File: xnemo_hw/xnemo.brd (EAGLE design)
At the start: 49.9 x 49 mm, 40 parts, among them J1 MICRO_USB_B_RECEPT, J2 DM3D_MICRO_SD, J3 HEADER_2X5_0.05_SMD, J4 HEADER_2X5_0.05_THRU, J5 HEADER_2X5_0.05_THRU, U1 LTC3559, U2 L3GD20, U3 STM32F405RG, U4 STM32F407VE, U5 HMC5883L, U6 ADXL345, X1 TXC_7A_XTAL

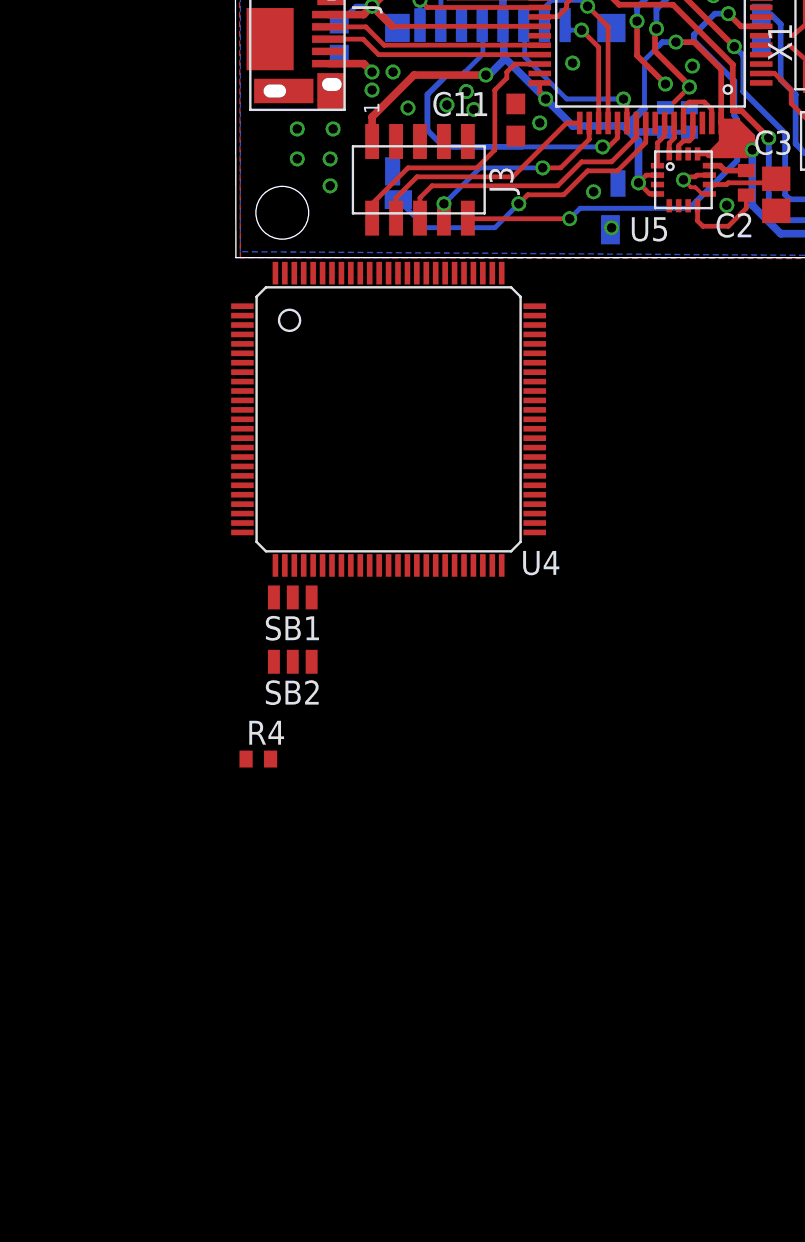
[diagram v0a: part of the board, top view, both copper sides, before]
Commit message: More junk added -- 2 compass units...
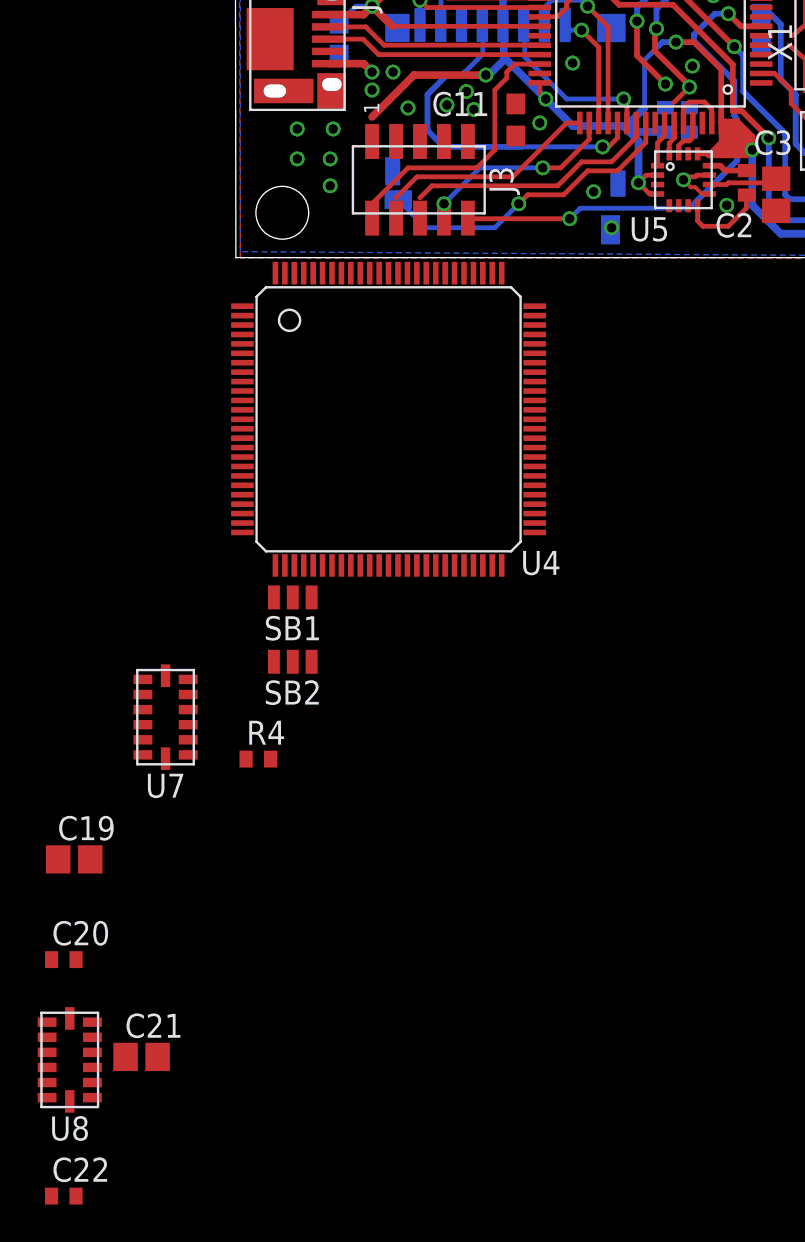
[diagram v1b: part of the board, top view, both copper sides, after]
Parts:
- added C19, C21: 4.7u, resistor:C0805
- added C20, C22: 0.22u, resistor:C0402
- added U7, U8: LSM303DLHC, xnemo:ST_LGA14_3X5
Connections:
- net N$1 renamed PDR_ON
- net N$16 renamed USART3_RX
- net N$17 renamed USART3_TX
- net N$18 renamed SPI2_MOSI
- net N$19 renamed SPI2_MISO
- net N$20 renamed SPI2_SCK
- net N$26 renamed I2S3_WS
- net N$39 renamed SPI1_MISO
- net N$40 renamed SPI1_MOSI
- net N$45 renamed DCMI_D2
- net N$46 renamed DCMI_D3
- net N$49 renamed DCMI_D4
- net N$50 renamed DCMI_D6
- net N$51 renamed DCMI_D7
- net N$68 renamed USART2_TX
- net N$69 renamed USART2_RX
- net N$72 renamed DCMI_HSYNC
- net N$73 renamed SPI1_SCK
- net N$74 renamed DCMI_PIXCLK
- net N$9 renamed DCMI_D0
- removed net N$2: U4.P$96
- removed net N$22: U4.P$72
- removed net N$25: U4.P$76
- removed net N$29: U4.P$80
- removed net N$32: U4.P$83
- removed net N$38: U4.P$89
- removed net N$4: U4.P$68
- removed net N$44: U4.P$95
- removed net N$56: U4.P$10
- removed net N$57: U4.P$11
- removed net N$90: U4.P$47
- removed net N$91: U4.P$48
- removed net SD_DAT0: J2.P$2, U3.P$39
- removed net SD_DAT1: J2.P$1, U3.P$40
- new net COMP1_DRDY: U7.P$9
- new net COMP1_INT1: U7.P$4
- new net COMP1_INT2: U7.P$5
- new net COMP2_DRDY: U8.P$9
- new net COMP2_INT1: U8.P$4
- new net COMP2_INT2: U8.P$5
- new net DCMI_D5: U4.P$92
- new net DCMI_VSYNC: U4.P$93
- new net I2C1_SCL: R6.1, U4.P$95, U7.P$2
- new net I2C1_SDA: R5.1, U4.P$96, U7.P$3
- new net I2C2_SCL: U4.P$47, U8.P$2
- new net I2C2_SDA: U4.P$48, U8.P$3
- new net N$23: C22.1, U8.P$13
- new net N$52: C19.2, U7.P$6
- new net NC: J3.7
- new net NRESET: J3.9, U4.P$14
- new net SD_DAT0_I2C3_SCL: J2.P$2, U3.P$39, U4.P$65
- new net SD_DAT1_I2C3_SDA: J2.P$1, U3.P$40, U4.P$66
- new net SWDCLK: J3.3, U4.P$76
- new net SWDIO: J3.1, U4.P$72
- new net SWO: J3.5, U4.P$89
- net 3V3: now also J3.2, U4.P$11, U7.P$1, U7.P$14, U8.P$1, U8.P$14; no longer J3.1
- net GND: now also C19.1, C21.1, J3.10, J3.4, J3.6, J3.8, U4.P$10, U7.P$10, U7.P$11, U7.P$7, U8.P$10, U8.P$11, U8.P$7; no longer J3.3, J3.5, J3.7, J3.9
- net I2C_SCL: no longer R6.1, U4.P$92
- net I2C_SDA: no longer R5.1, U4.P$93
- net JTCK: no longer J3.4
- net JTDI: no longer J3.8
- net JTDO: no longer J3.6
- net JTMS: no longer J3.2
- net N$27: now also C20.1, U7.P$13; no longer U4.P$78
- net N$28: now also C21.2, U8.P$6; no longer U4.P$79
- net N$6: now also C22.2, U8.P$12; no longer U4.P$66
- net N$7: now also C20.2, U7.P$12; no longer U4.P$65
- net RESET: no longer J3.10, U4.P$14
- net SD_CLK: now also U4.P$80
- net SD_CMD: now also U4.P$83
- net SD_DAT2: now also U4.P$78
- net SD_DAT3: now also U4.P$79
- net VUSB: now also U4.P$68
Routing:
- net SD_DAT1_I2C3_SDA: track 0.00 -> 7.83 mm, vias 0 -> 1
- net SD_DAT1: track 7.83 -> 0.00 mm, vias 1 -> 0
- net SD_DAT0_I2C3_SCL: track 0.00 -> 7.19 mm, vias 0 -> 1
- net SD_DAT0: track 7.19 -> 0.00 mm, vias 1 -> 0
- net 3V3: track 184.8 -> 182.2 mm
- net JTCK: track 12.5 -> 11.4 mm
- net JTDO: track 14.6 -> 13.6 mm
- net JTMS: track 14.8 -> 14.0 mm
- net JTDI: track 10.7 -> 9.99 mm

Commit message: Started routing
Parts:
- removed C18: 0.1u, resistor:C0402
- removed J5: HEADER_2X5_0.05_THRU, xnemo:HEADER_2X5_0.05_THRU
- removed U3: STM32F405RG, xnemo:ST_LQFP64
- removed U5: HMC5883L, xnemo:HW_LCC16_3X3
- removed U6: ADXL345, xnemo:AD_LGA14_3X5
- added C23: 10n, resistor:C0402
- added C24: 0.22u, resistor:C0402
- added C25: 10u, resistor:C0805
- added R7: 33k, resistor:R0402
- added R8, R9: 22k, resistor:R0402
- added U10: STTS751, xnemo:ST_UDFN-6L_2X2
- added U9: L3GD20, xnemo:ST_LGA16_4X4
- C17: value 10u -> 2.2u; device resistor:C0805 -> resistor:C0603
- C2: value 0.22u -> 10u; device resistor:C0402 -> resistor:C0805
- C3: value 4.7u -> 2.2u; device resistor:C0805 -> resistor:C0603
- J4: value HEADER_2X5_0.05_THRU -> HEADER_2X7; device xnemo:HEADER_2X5_0.05_THRU -> xnemo:HEADER_2X7_0.05X0.1_THRU
- moved C19 77.3 mm to (10.8, 42.9), turned to 270 degrees
- moved C20 75.1 mm to (5.87, 36.3), turned to 90 degrees
- moved R4 66.9 mm to (21.7, 37.0), turned to 90 degrees
- moved U7 63.8 mm to (9.21, 38.0), turned to 180 degrees
- moved C22 60.1 mm to (17.2, 4.13), turned to 90 degrees
- moved C21 59.2 mm to (26.0, 7.94), turned to 180 degrees
- moved U8 56.6 mm to (20.3, 5.79), turned to 180 degrees
- moved SB1 56.3 mm to (18.7, 36.0)
- moved J1 49.1 mm to (48.2, 27.8), turned to 90 degrees
- moved J3 47.4 mm to (31.1, 46.3)
- moved C7 43.8 mm to (45.9, 27.9), turned to 270 degrees
- moved C8 41.8 mm to (39.4, 44.2), flipped to the bottom, turned to 0 degrees
- moved SB2 40.8 mm to (9.68, 18.8), turned to 90 degrees
- moved J2 40.0 mm to (27.1, 43.9), turned to 0 degrees
- moved C14 39.9 mm to (45.6, 37.5), flipped to the top, turned to 0 degrees
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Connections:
- net GYR_RES renamed GYR_RES1
- net N$21 renamed SPI2_NSS_WS
- net N$28 renamed COMP2_C1
- net N$52 renamed COMP1_C1
- net SPI2_MISO renamed SPI2_MISO_EXT_SD
- net SPI2_MOSI renamed SPI2_MOSI_SD
- net SPI2_SCK renamed SPI2_SCK_CK
- removed net ACC_INT1: U3.P$27, U6.P$8
- removed net ACC_INT2: U3.P$26, U6.P$9
- removed net DCMI_D0: U4.P$63
- removed net GYR_DRDY: U2.P$6, U3.P$38
- removed net GYR_INT1: U2.P$7, U3.P$37
- removed net I2C_SCL: J4.P$5, U5.P$1
- removed net I2C_SDA: J4.P$9, U5.P$16
- removed net JTCK: U3.P$49
- removed net JTDI: U3.P$50
- removed net JTDO: U3.P$55
- removed net JTMS: U3.P$46
- removed net MAG_C1: C3.1, U5.P$10
- removed net MAG_DRDY: U3.P$61, U5.P$15
- removed net MAG_SETC: C2.2, U5.P$12
- removed net MAG_SETP: C2.1, U5.P$8
- removed net N$24: U4.P$75
- removed net N$30: U4.P$81
- removed net N$31: U4.P$82
- removed net N$33: U4.P$84
- removed net N$34: U4.P$85
- removed net N$35: U4.P$86
- removed net N$36: U4.P$87
- removed net N$37: U4.P$88
- removed net N$59: U4.P$16
- removed net N$60: U4.P$17
- removed net N$61: U4.P$18
- removed net N$63: U4.P$20
- removed net N$70: U4.P$27
- removed net N$71: U4.P$28
- removed net N$84: U4.P$41
- removed net N$85: U4.P$42
- removed net N$86: U4.P$43
- removed net N$87: U4.P$44
- removed net N$88: U4.P$45
- removed net N$89: U4.P$46
- removed net N$9: U4.P$64
- removed net N$93: U4.P$50
- removed net PA0: J4.P$8, U3.P$14
- removed net PA1: J4.P$6, U3.P$15
- removed net PA10: U3.P$43
- removed net PA2: J4.P$2, U3.P$16
- removed net PA3: J4.P$1, U3.P$17
- removed net PA4: J4.P$10, U3.P$20
- removed net PB12: J5.P$9, U3.P$33
- removed net PB13: J5.P$10, U3.P$34
- removed net PB14: J5.P$4, U3.P$35
- removed net PB15: J5.P$6, U3.P$36
- removed net PC0: U3.P$8
- removed net PC1: U3.P$9
- removed net PC13: J5.P$1, U3.P$2
- removed net PC2: U3.P$10
- removed net PC3: U3.P$11
- removed net PC4: J4.P$7, U3.P$24
- removed net RESET: U3.P$7
- removed net SPI_CLK: U2.P$2, U3.P$21, U6.P$14
- removed net SPI_CS_ACC: U3.P$25, U6.P$7
- removed net SPI_CS_GYR: U2.P$5, U3.P$41
- removed net SPI_MISO: U2.P$4, U3.P$22, U6.P$12
- removed net SPI_MOSI: U2.P$3, U3.P$23, U6.P$13
- new net DCMI_D0_MCK: J4.P$4, U4.P$63
- new net DCMI_D1: J4.P$6, U4.P$64
- new net GYR1_DRDY: U2.P$6, U4.P$17
- new net GYR1_INT1: U2.P$7, U4.P$18
- new net GYR2_DRDY: U4.P$45, U9.P$6
- new net GYR2_INT1: U4.P$44, U9.P$7
- new net GYR_RES2: C23.2, U9.P$14
- new net SPI_CS_GYR1: U2.P$5, U4.P$16
- new net SPI_CS_GYR2: U4.P$46, U9.P$5
- new net TEMP1_ADDR: R7.1, U10.P$4
- new net TEMP1_EVT: U10.P$2
- net 3V3: now also C17.2, C2.1, C24.2, C25.1, C3.1, J4.P$11, R7.2, R8.2, R9.2, U10.P$3, U4.P$28, U4.P$50, U4.P$75, U9.P$1, U9.P$15, U9.P$16; no longer C17.1, C18.2, J4.P$4, J5.P$2, J5.P$8, U3.P$19, U3.P$32, U3.P$48, U3.P$64, U5.P$13, U5.P$2, U5.P$4, U6.P$1, U6.P$6
- net COMP1_DRDY: now also U4.P$88
- net COMP1_INT1: now also U4.P$86
- net COMP1_INT2: now also U4.P$87
- net COMP2_DRDY: now also U4.P$41
- net COMP2_INT1: now also U4.P$43
- net COMP2_INT2: now also U4.P$42
- net DCMI_D2: now also J4.P$8
- net DCMI_D3: now also J4.P$10
- net DCMI_D4: now also J4.P$12
- net DCMI_D5: now also J4.P$14
- net DCMI_D6: now also J4.P$1
- net DCMI_D7: now also J4.P$3
- net DCMI_HSYNC: now also J4.P$9
- net DCMI_PIXCLK: now also J4.P$5
- net DCMI_VSYNC: now also J4.P$7
- net GND: now also C17.1, C2.2, C23.1, C24.1, C25.2, J4.P$13, J4.P$2, U10.P$5, U4.P$20, U4.P$27, U9.P$10, U9.P$11, U9.P$12, U9.P$13, U9.P$8, U9.P$9; no longer C17.2, C18.1, J4.P$3, J5.P$3, J5.P$5, J5.P$7, U3.P$18, U3.P$60, U3.P$63, U5.P$11, U5.P$9, U6.P$2, U6.P$4, U6.P$5
- net I2C1_SCL: now also U10.P$1
- net I2C1_SDA: now also U10.P$6
- net I2C2_SCL: now also R9.1
- net I2C2_SDA: now also R8.1
- net POW_CHRG: now also U4.P$81; no longer U3.P$28
- net POW_HPWR: now also U4.P$82; no longer U3.P$29
- net POW_SUSP: now also U4.P$85; no longer U3.P$30
- net SD_CLK: no longer U3.P$53
- net SD_CMD: no longer U3.P$54
- net SD_DAT0_I2C3_SCL: no longer U3.P$39
- net SD_DAT1_I2C3_SDA: no longer U3.P$40
- net SD_DAT2: no longer U3.P$51
- net SD_DAT3: no longer U3.P$52
- net SD_DET: now also U4.P$84; no longer U3.P$56
- net SPI1_MISO: now also U2.P$4, U9.P$4
- net SPI1_MOSI: now also U2.P$3, U9.P$3
- net SPI1_SCK: now also U2.P$2, U9.P$2
- net USB_D+: no longer U3.P$45
- net USB_D-: no longer U3.P$44
- net VUSB: no longer U3.P$42
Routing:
- net 3V3: track 182.2 -> 74.3 mm, vias 12 -> 0
- net I2C_SCL: track 34.9 -> 0.00 mm, vias 3 -> 0
- net SWDIO: track 0.00 -> 33.2 mm
- net PB12: track 33.1 -> 0.00 mm, vias 6 -> 0
- net COMP1_DRDY: track 0.00 -> 31.9 mm, vias 0 -> 2
- net PB13: track 30.6 -> 0.00 mm, vias 1 -> 0
- net I2C_SDA: track 30.5 -> 0.00 mm, vias 2 -> 0
- net DCMI_D0_MCK: track 0.00 -> 30.2 mm, vias 0 -> 1
- net DCMI_D1: track 0.00 -> 30.1 mm, vias 0 -> 1
- net I2C1_SCL: track 0.00 -> 29.9 mm, vias 0 -> 3
- net PB15: track 29.3 -> 0.00 mm, vias 1 -> 0
- net SPI_CS_ACC: track 27.5 -> 0.00 mm, vias 2 -> 0
- net RESET: track 27.2 -> 0.00 mm, vias 2 -> 0
- net PB14: track 26.4 -> 0.00 mm, vias 1 -> 0
- net DCMI_HSYNC: track 0.00 -> 25.6 mm, vias 0 -> 1
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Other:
- board size 49.9 x 49 mm -> 49.8 x 49.8 mm
- board text removed: "bnahill@gmail.com"
- board text removed: "xNEMO r1"

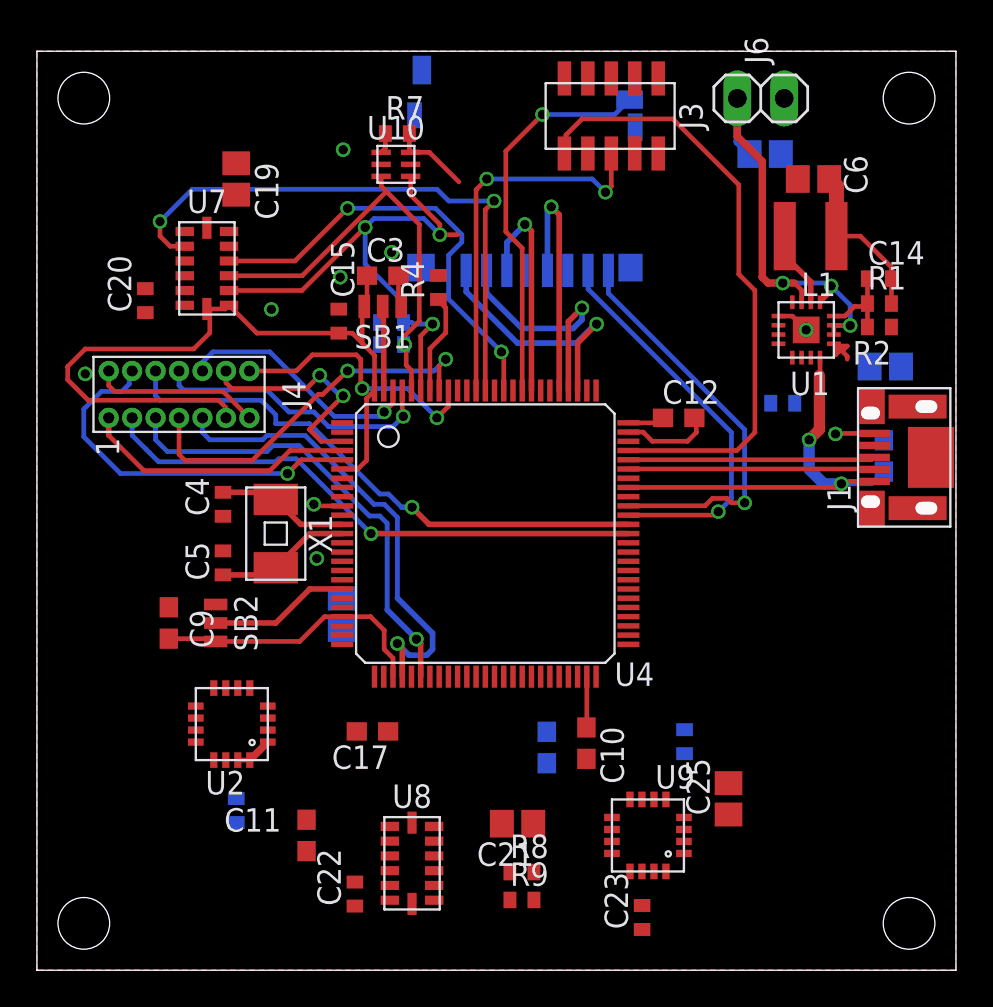
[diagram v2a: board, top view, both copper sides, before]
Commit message: Added datasheet, fixed some footprints
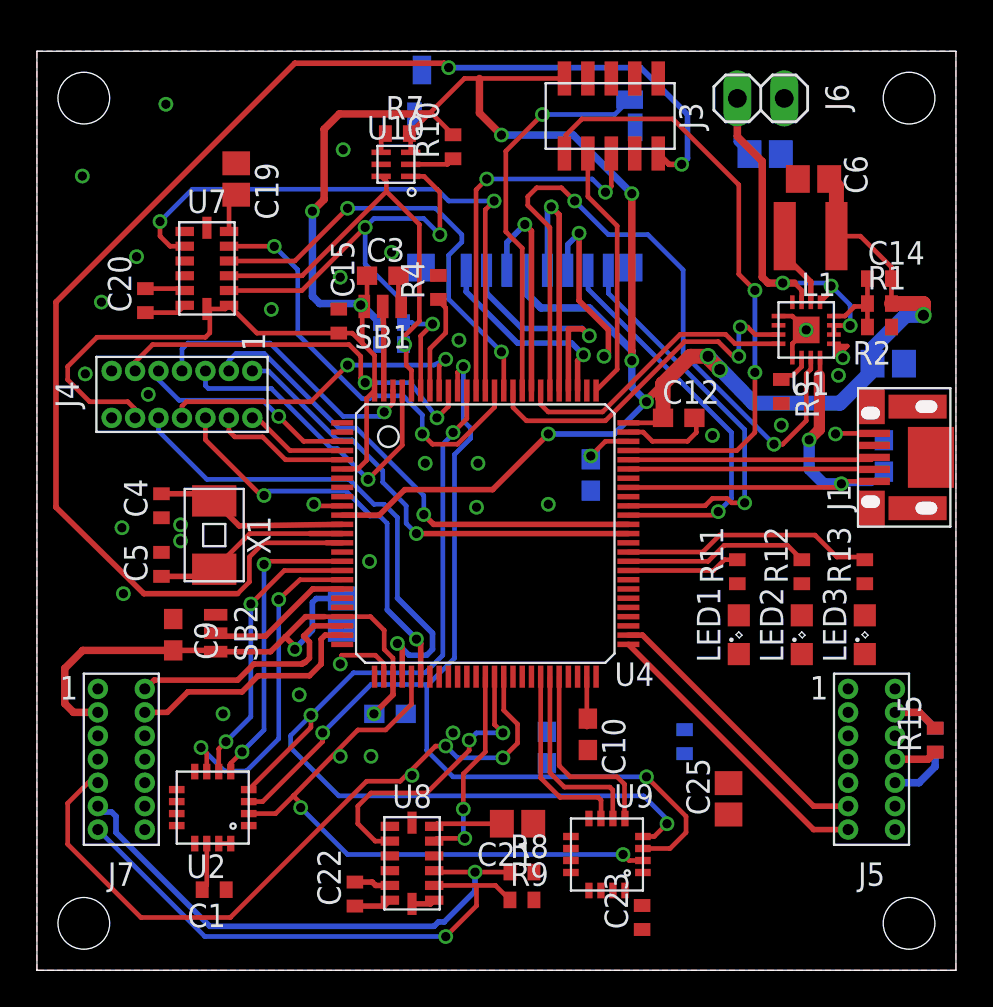
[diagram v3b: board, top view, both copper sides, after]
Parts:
- added J5, J7: HEADER_2X7, xnemo:HEADER_2X7_0.05X0.1_THRU
- added LED1, LED2, LED3: (no value), led:SML0805
- added R10: 33k, resistor:R0402
- added R11, R12, R13: 680, resistor:R0402
- added R14, R15: 22k, resistor:R0402
- moved C11 24.9 mm to (30.0, 26.8), flipped to the bottom
- moved U2 4.64 mm to (9.53, 8.81)
- moved C1 4.45 mm to (9.60, 4.37), flipped to the top, turned to 180 degrees
- moved X1 3.33 mm to (9.60, 23.6)
- moved C4 3.33 mm to (6.75, 25.2)
- moved C5 3.33 mm to (6.75, 22.0)
- moved U9 2.45 mm to (30.9, 6.27)
- moved J4 2.38 mm to (6.59, 31.2), turned to 270 degrees
- moved C17 1.35 mm to (19.1, 13.9), flipped to the bottom, turned to 0 degrees
- moved C9 0.68 mm to (7.38, 18.2)
- moved R3 0.64 mm to (40.3, 31.4), flipped to the top, turned to 270 degrees
- moved SB2 0.56 mm to (9.68, 18.3)
- moved C10 0.48 mm to (29.8, 12.8)
- moved C2 0.22 mm to (46.1, 32.9), turned to 180 degrees
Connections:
- removed net N$1: U4.P$24
- removed net N$11: U4.P$61
- removed net N$12: U4.P$60
- removed net N$13: U4.P$59
- removed net N$15: U4.P$57
- removed net N$66: U4.P$23
- removed net N$75: U4.P$32
- removed net N$76: U4.P$33
- removed net N$77: U4.P$34
- removed net N$78: U4.P$35
- removed net N$79: U4.P$36
- removed net N$81: U4.P$38
- removed net N$82: U4.P$39
- removed net N$83: U4.P$40
- new net LED1: R11.2, U4.P$59
- new net LED2: R12.2, U4.P$60
- new net LED3: R13.2, U4.P$61
- new net N$16: LED2.A, R12.1
- new net N$17: LED3.A, R13.1
- new net N$8: LED1.C, LED2.C, LED3.C
- new net N$9: LED1.A, R11.1
- new net PA0: J7.2, U4.P$23
- new net PA1: J7.4, U4.P$24
- new net PA7: J7.6, U4.P$32
- new net PB0: J7.12, U4.P$35
- new net PB1: J7.14, U4.P$36
- new net PC4: J7.8, U4.P$33
- new net PC5: J7.10, U4.P$34
- new net PE11: J7.7, U4.P$42
- new net PE13: J7.5
- new net PE9: J7.9, U4.P$40
- new net USART3_CK: J5.1, U4.P$57
- net 3V3: now also J4.12, J5.4, J7.3, R10.2, R14.2, R15.2, U10.3; no longer J4.P$11, U10.P$3
- net COMP2_DRDY: now also U4.P$39; no longer U4.P$41
- net COMP2_INT2: now also U4.P$38; no longer U4.P$42
- net DCMI_D0_MCK: now also J4.1, J5.6; no longer J4.P$4
- net DCMI_D1: now also J4.3; no longer J4.P$6
- net DCMI_D2: now also J4.5; no longer J4.P$8
- net DCMI_D3: now also J4.7; no longer J4.P$10
- net DCMI_D4: now also J4.9; no longer J4.P$12
- net DCMI_D5: now also J4.11; no longer J4.P$14
- net DCMI_D6: now also J4.2; no longer J4.P$1
- net DCMI_D7: now also J4.4; no longer J4.P$3
- net DCMI_HSYNC: now also J4.10; no longer J4.P$9
- net DCMI_PIXCLK: now also J4.6; no longer J4.P$5
- net DCMI_VSYNC: now also J4.8; no longer J4.P$7
- net GND: now also J4.13, J4.14, J5.14, J7.1, U10.5; no longer J4.P$13, J4.P$2, U10.P$5
- net I2C1_SCL: now also U10.1; no longer U10.P$1
- net I2C1_SDA: now also U10.6; no longer U10.P$6
- net I2C2_SCL: now also J7.13
- net I2C2_SDA: now also J7.11
- net SD_DAT0_I2C3_SCL: now also J5.10, R14.1
- net SD_DAT1_I2C3_SDA: now also J5.8, R15.1
- net SPI2_MISO_EXT_SD: now also J5.9
- net SPI2_MOSI_SD: now also J5.7
- net SPI2_NSS_WS: now also J5.13
- net SPI2_SCK_CK: now also J5.11
- net TEMP1_ADDR: now also U10.4; no longer U10.P$4
- net TEMP1_EVT: now also R10.1, U10.2; no longer U10.P$2
- net USART3_RX: now also J5.3
- net USART3_TX: now also J5.5
- net VBAT: now also J5.12
- net VUSB: now also J5.2
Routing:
- net 3V3: track 74.3 -> 197.3 mm, vias 0 -> 12
- net NRESET: track 0.00 -> 75.5 mm, vias 0 -> 2
- net SPI1_MOSI: track 0.00 -> 55.1 mm, vias 0 -> 3
- net SPI1_MISO: track 0.00 -> 54.8 mm, vias 0 -> 3
- net POW_CHRG: track 0.00 -> 38.7 mm, vias 0 -> 2
- net PE9: track 0.00 -> 38.7 mm, vias 0 -> 2
- net SPI1_SCK: track 0.00 -> 33.3 mm, vias 0 -> 2
- net I2C2_SDA: track 0.00 -> 29.6 mm, vias 0 -> 1
- net I2C2_SCL: track 0.00 -> 29.1 mm, vias 0 -> 1
- net COMP1_INT2: track 0.00 -> 23.3 mm, vias 0 -> 2
- net POW_SUSP: track 0.00 -> 19.4 mm, vias 0 -> 2
- net GYR1_INT1: track 0.00 -> 18.3 mm, vias 0 -> 2
- net SPI_CS_GYR1: track 0.00 -> 16.3 mm, vias 0 -> 2
- net COMP2_DRDY: track 0.00 -> 16.1 mm, vias 0 -> 2
- net SPI2_NSS_WS: track 0.00 -> 16.1 mm
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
